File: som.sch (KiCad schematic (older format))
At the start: 18 parts, among them M1 SC606T

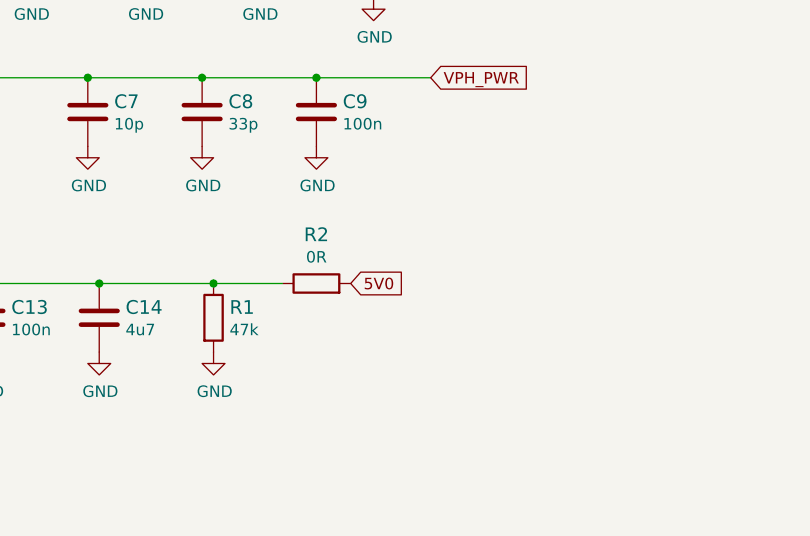
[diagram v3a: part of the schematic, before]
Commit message: Added 5V to 4V SoM power supply and 5V to 3V3 camera power supply
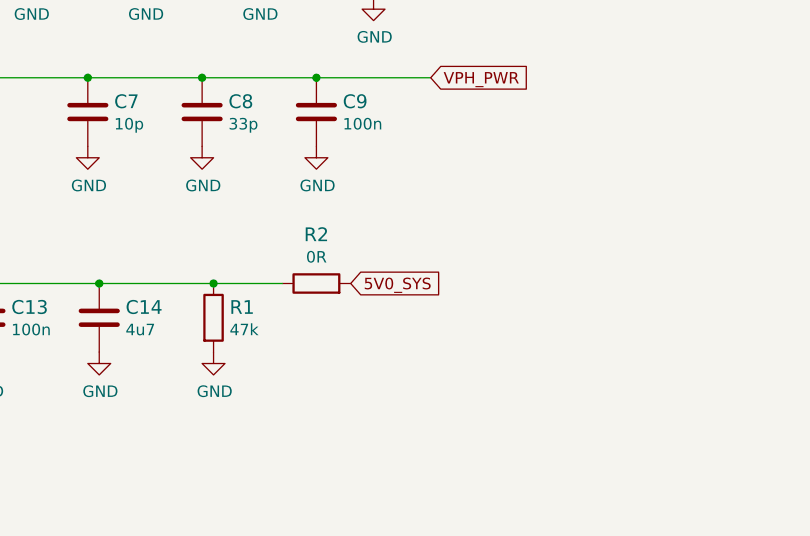
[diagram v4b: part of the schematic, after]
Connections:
- net 5V0 renamed 5V0_SYS
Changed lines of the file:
@@
 $EndComp
 Text GLabel 5900 9650 2    50   Input ~ 0
-5V0
+5V0_SYS
 $Comp
 L power:GND #PWR?

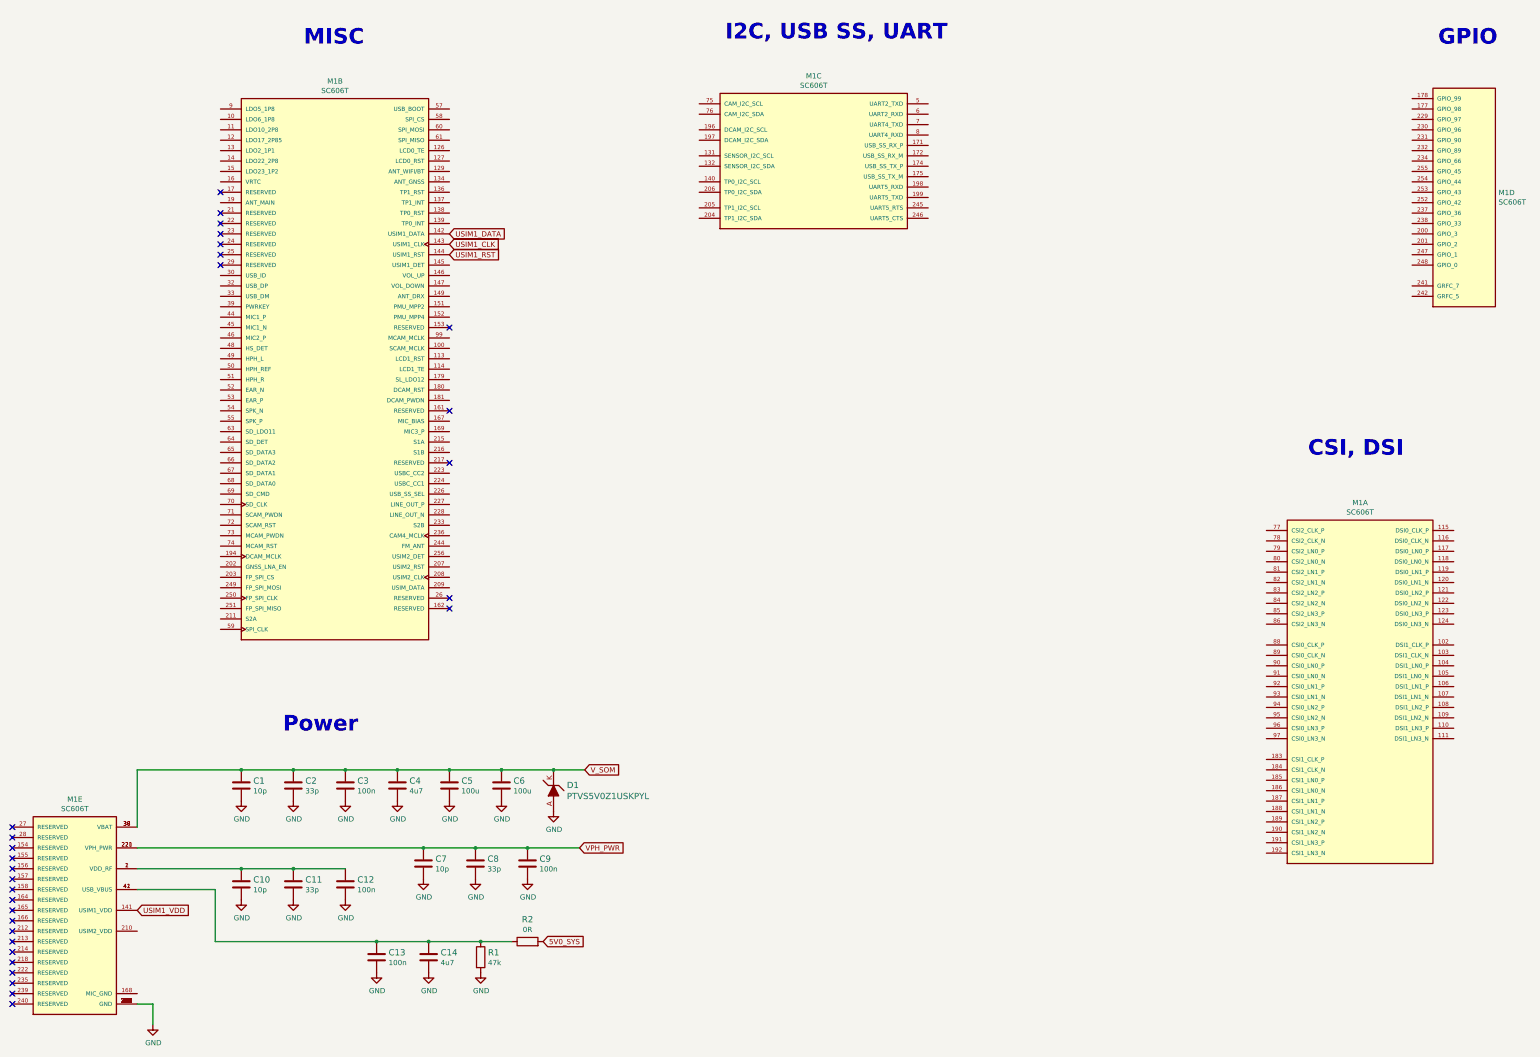
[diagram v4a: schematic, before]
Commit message: Creating schemas for camera FFC, connecting related pins to SoM, schema of I2C MUX and voltage transceiver; Adding RESET to power supplies; connecting to SoM 1v8 power output
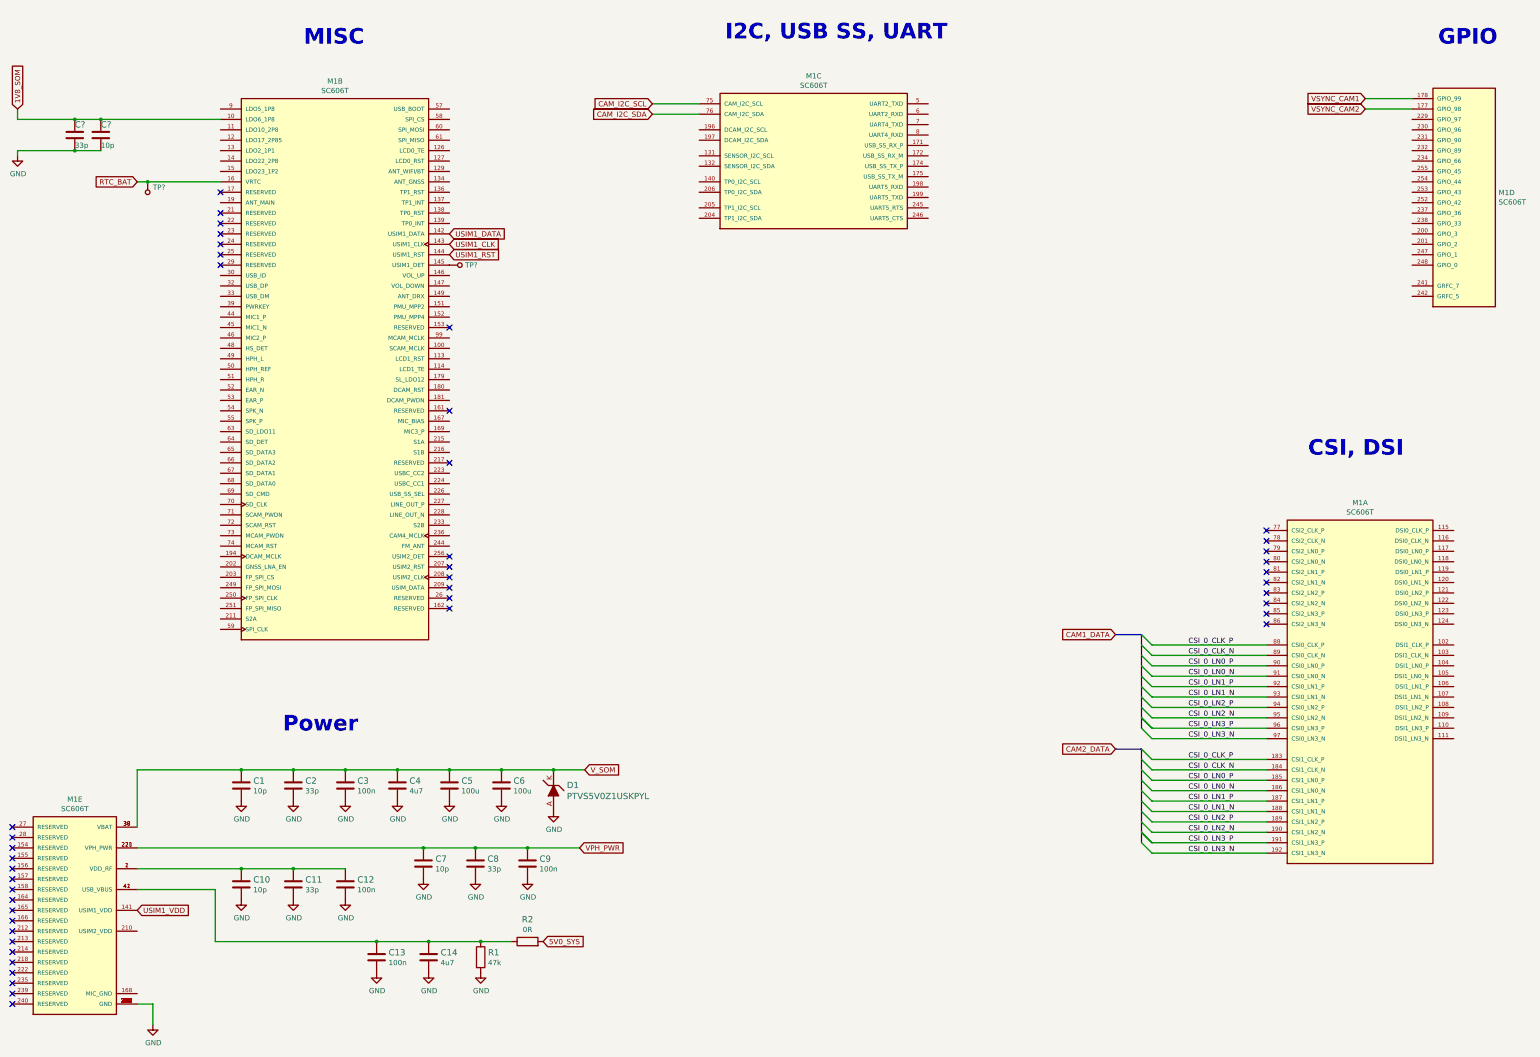
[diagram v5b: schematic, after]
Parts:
- added C?: C_33p_0402, antmicro-footprints:0402-cap, symbol antmicroCapacitors0402:C_33p_0402
- added C?: C_10p_0402, antmicro-footprints:0402-cap, symbol antmicroCapacitors0402:C_10p_0402
- added TP? (x2): TP_SMD_0_75MM, antmicro-footprints:Testpoint_smd_0_75mm, symbol antmicroTestPoints:TP_SMD_0_75MM
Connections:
- net GND: now also C?.2, C?.2
- net CSI_0_CLK_P: now reaches M1.183 (CSI1_CLK_P)
- net CSI_0_CLK_P: now also M1.88 (CSI0_CLK_P)
- net CSI_0_CLK_N: now reaches M1.184 (CSI1_CLK_N)
- net CSI_0_CLK_N: now also M1.89 (CSI0_CLK_N)
- net CSI_0_LN0_P: now reaches M1.185 (CSI1_LN0_P)
- net CSI_0_LN0_P: now also M1.90 (CSI0_LN0_P)
- net CSI_0_LN0_N: now reaches M1.186 (CSI1_LN0_N)
- net CSI_0_LN0_N: now also M1.91 (CSI0_LN0_N)
- net CSI_0_LN1_P: now reaches M1.187 (CSI1_LN1_P)
- net CSI_0_LN1_P: now also M1.92 (CSI0_LN1_P)
- net CSI_0_LN1_N: now reaches M1.188 (CSI1_LN1_N)
- net CSI_0_LN1_N: now also M1.93 (CSI0_LN1_N)
- net CSI_0_LN2_P: now reaches M1.189 (CSI1_LN2_P)
- net CSI_0_LN2_P: now also M1.94 (CSI0_LN2_P)
- net CSI_0_LN2_N: now reaches M1.190 (CSI1_LN2_N)
- net CSI_0_LN2_N: now also M1.95 (CSI0_LN2_N)
- net CSI_0_LN3_P: now reaches M1.191 (CSI1_LN3_P)
- net CSI_0_LN3_P: now also M1.96 (CSI0_LN3_P)
- net CSI_0_LN3_N: now reaches M1.192 (CSI1_LN3_N)
- net CSI_0_LN3_N: now also M1.97 (CSI0_LN3_N)
- net 1V8_SOM: now reaches M1.10 (LDO6_1P8)
- net 1V8_SOM: now also C?.1, C?.1
- net at M1.145 (USIM1_DET): now also TP?.1
- net RTC_BAT: now reaches M1.16 (VRTC)
- net RTC_BAT: now also TP?.1
- net CAM_I2C_SCL: now reaches M1.75 (CAM_I2C_SCL)
- net CAM_I2C_SDA: now reaches M1.76 (CAM_I2C_SDA)
- net VSYNC_CAM2: now reaches M1.177 (GPIO_98)
- net VSYNC_CAM1: now reaches M1.178 (GPIO_99)
- no-connect marks 30 -> 44

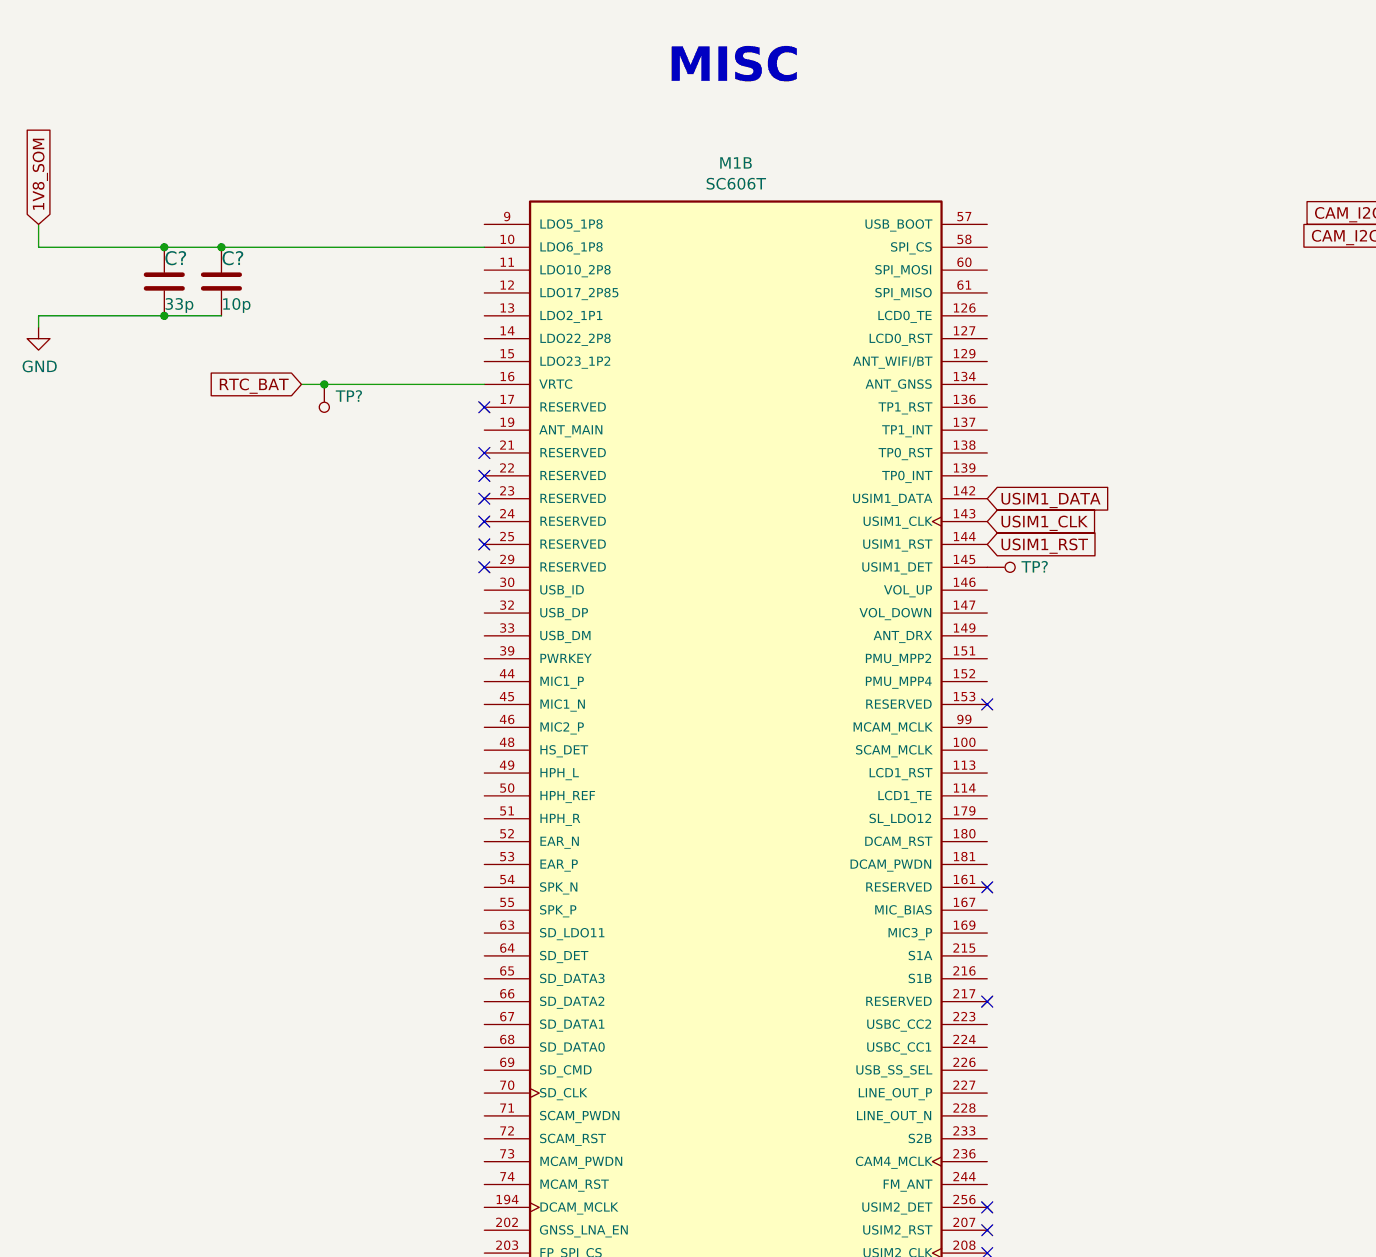
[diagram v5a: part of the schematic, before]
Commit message: Creating schema for SD card connection
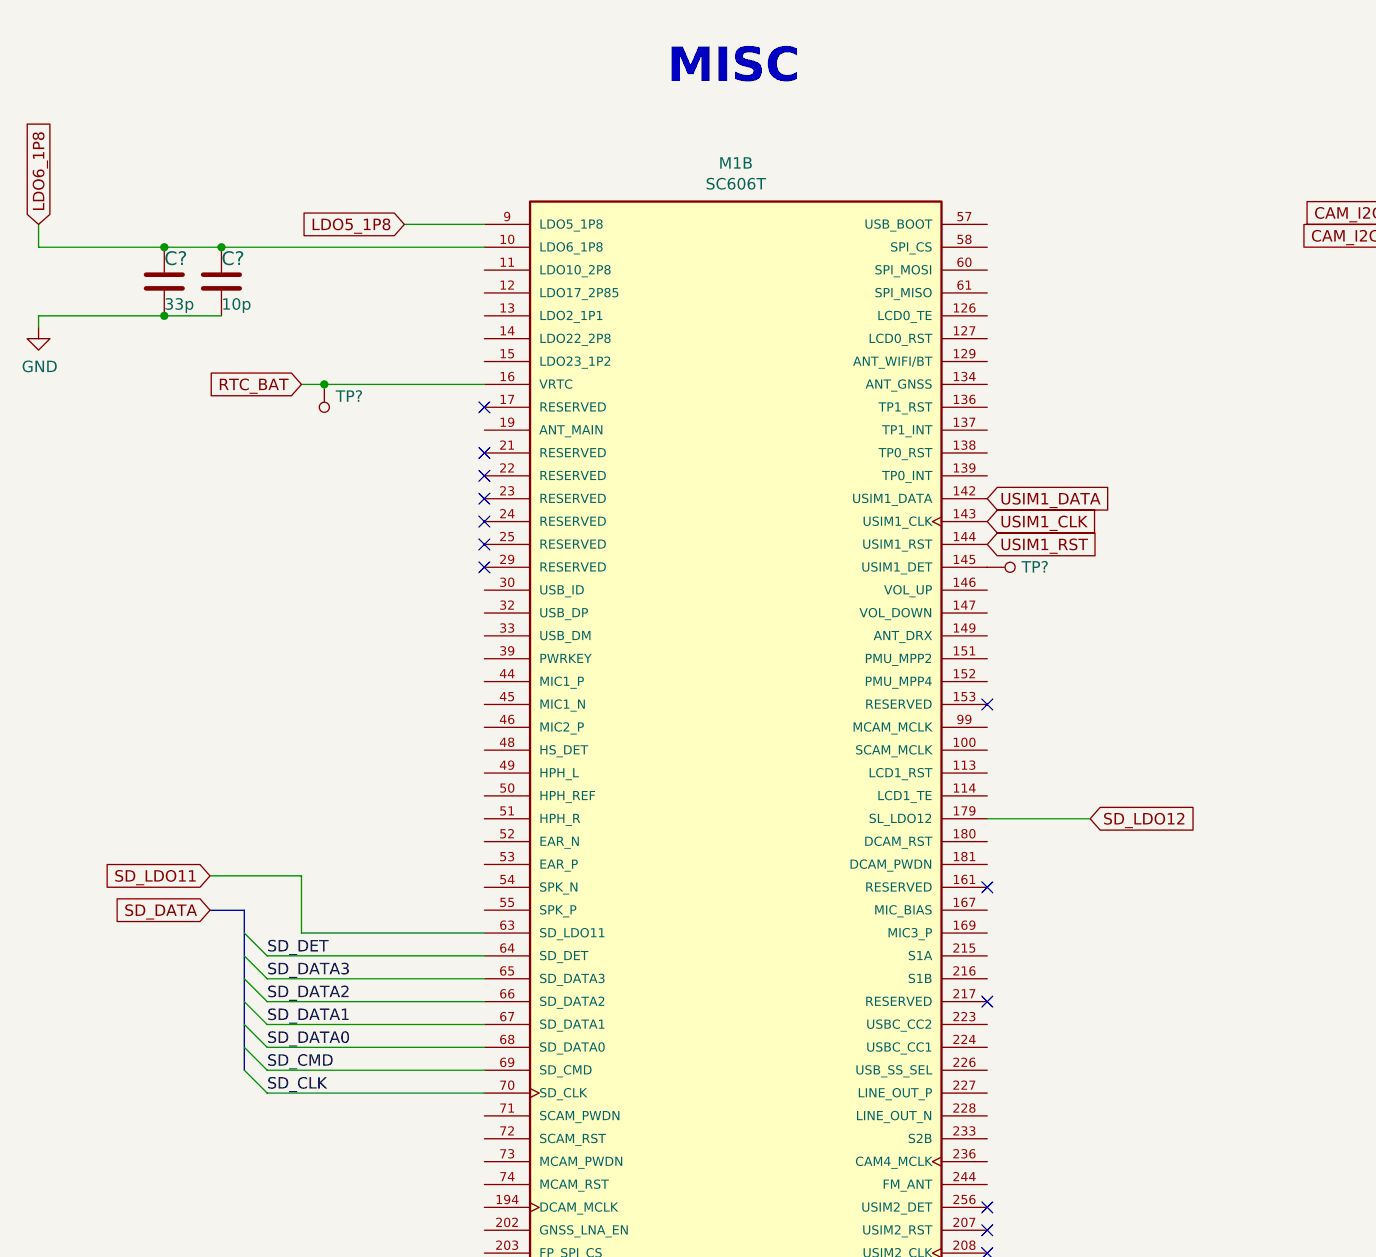
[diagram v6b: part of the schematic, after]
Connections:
- net SD_LDO12: now reaches M1.179 (SL_LDO12)
- net SD_LDO11: now reaches M1.63 (SD_LDO11)
- net SD_DET: now reaches M1.64 (SD_DET)
- net SD_DATA3: now reaches M1.65 (SD_DATA3)
- net SD_DATA2: now reaches M1.66 (SD_DATA2)
- net SD_DATA1: now reaches M1.67 (SD_DATA1)
- net SD_DATA0: now reaches M1.68 (SD_DATA0)
- net SD_CMD: now reaches M1.69 (SD_CMD)
- net SD_CLK: now reaches M1.70 (SD_CLK)
- net LDO5_1P8: now reaches M1.9 (LDO5_1P8)
- net 1V8_SOM renamed LDO6_1P8
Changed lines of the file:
@@
 	2000 2350 2100 2350
 Text GLabel 850  1650 1    50   Input ~ 0
-1V8_SOM
+LDO6_1P8
 $Comp
 L antmicroCapacitors0402:C_33p_0402 C?
@@
 NoConn ~ 5000 6150
 NoConn ~ 5000 6250
+Text Label 1850 4850 0    50   ~ 0
+SD_DET
+Text Label 1850 4950 0    50   ~ 0
+SD_DATA3
+Text Label 1850 5050 0    50   ~ 0
+SD_DATA2
+Text Label 1850 5150 0    50   ~ 0
+SD_DATA1
+Text Label 1850 5250 0    50   ~ 0
+SD_DATA0
+Text Label 1850 5350 0    50   ~ 0
+SD_CMD
+Text Label 1850 5450 0    50   ~ 0
+SD_CLK
+Wire Wire Line
+	1850 4850 2800 4850
+Wire Wire Line
+	2800 4950 1850 4950
+Wire Wire Line
+	1850 5050 2800 5050
+Wire Wire Line
+	2800 5150 1850 5150
+Wire Wire Line
+	1850 5250 2800 5250
+Wire Wire Line
+	2800 5350 1850 5350
+Wire Wire Line
+	1850 5450 2800 5450
+Entry Wire Line
+	1750 4750 1850 4850
+Entry Wire Line
+	1750 4850 1850 4950
+Entry Wire Line
+	1750 4950 1850 5050
+Entry Wire Line
+	1750 5050 1850 5150
+Entry Wire Line
+	1750 5150 1850 5250
+Entry Wire Line
+	1750 5250 1850 5350
+Entry Wire Line
+	1750 5350 1850 5450
+Wire Bus Line
+	1750 4650 1600 4650
+Text GLabel 1600 4650 0    50   Input ~ 0
+SD_DATA
+Text GLabel 1600 4500 0    50   Input ~ 0
+SD_LDO11
+Wire Wire Line
+	2800 4750 2000 4750
+Wire Wire Line
+	2000 4750 2000 4500
+Wire Wire Line
+	1600 4500 2000 4500
+Text GLabel 5450 4250 2    50   Input ~ 0
+SD_LDO12
+Wire Wire Line
+	5450 4250 5000 4250
+Text GLabel 2450 1650 0    50   Input ~ 0
+LDO5_1P8
+Wire Wire Line
+	2450 1650 2800 1650
+Wire Bus Line
+	1750 4650 1750 5350
 Wire Bus Line
 	11650 6700 11650 7600

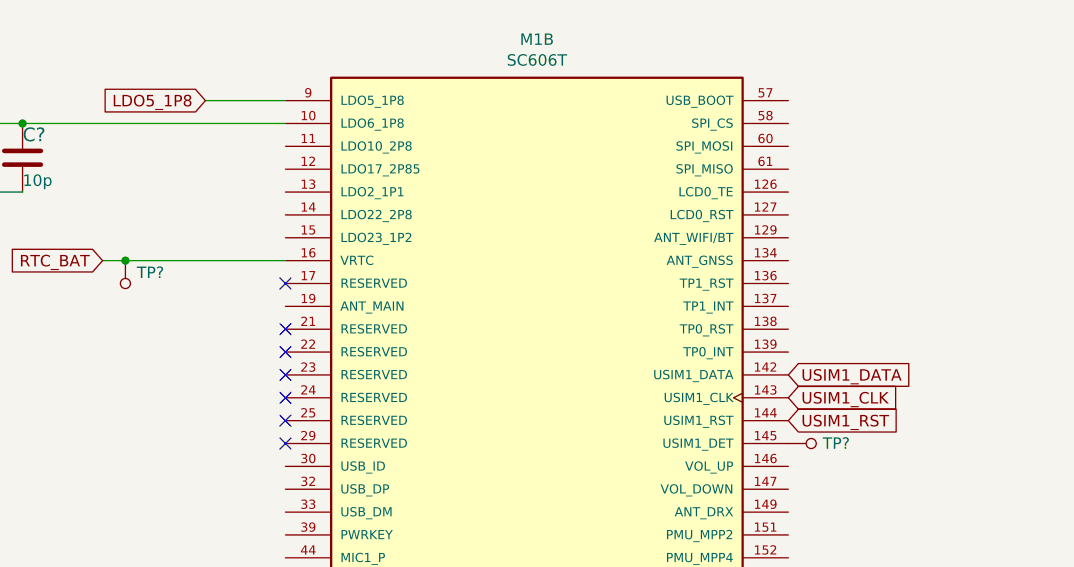
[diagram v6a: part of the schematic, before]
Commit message: Added schema of Main and GNSS Antenna
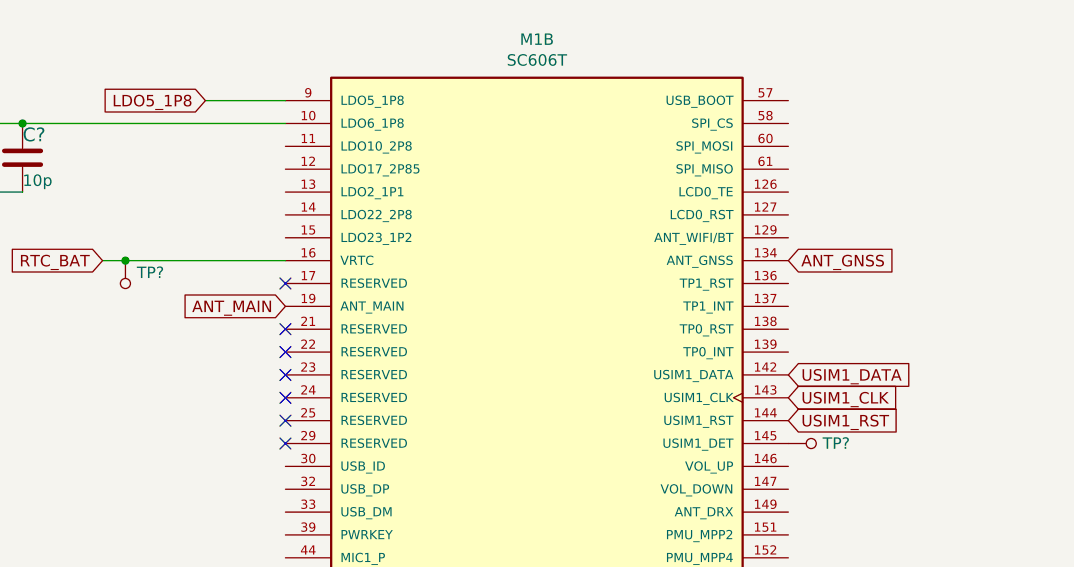
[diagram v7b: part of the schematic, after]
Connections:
- net ANT_GNSS: now reaches M1.134 (ANT_GNSS)
- net ANT_MAIN: now reaches M1.19 (ANT_MAIN)
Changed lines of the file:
@@
 Wire Bus Line
 	11650 7800 11650 8700
+Text GLabel 5000 2350 2    50   Input ~ 0
+ANT_GNSS
+Text GLabel 2800 2550 0    50   Input ~ 0
+ANT_MAIN
 $EndSCHEMATC
